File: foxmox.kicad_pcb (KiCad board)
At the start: 2 copper layers, 63.5 x 63.5 mm, 17 parts, among them P1 2.5mm plug, Q1 2N2222A, U1 PIC16F84, Y1 3.579MHz

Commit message: Slightly better PCB
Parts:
- D1: footprint Diode_SMD:D_MiniMELF -> Diode_THT:D_A-405_P10.16mm_Horizontal
- P1: footprint TerminalBlock:TerminalBlock_MaiXu_MX126-5.0-03P_1x03_P5.00mm -> TerminalBlock_CUI:TerminalBlock_CUI_TB007-508-03_1x03_P5.08mm_Horizontal
- R2: footprint Potentiometer_THT:Potentiometer_Piher_PT-15-H01_Horizontal -> Potentiometer_THT:Potentiometer_Bourns_3266W_Vertical
- moved C4 52.1 mm to (134.1, 67.5)
- moved S3 47.6 mm to (122.6, 68.4)
- moved Q1 37.1 mm to (143.0, 73.0)
- moved C3 31.4 mm to (149.5, 67.5)
- moved P1 28.9 mm to (120.0, 84.9), turned to -90 degrees
- moved D1 23.0 mm to (151.8, 92.5)
- moved R4 20.4 mm to (115.4, 101.5)
- moved R2 18.7 mm to (158.8, 67.5), turned to 90 degrees
- moved Y1 18.3 mm to (159.1, 99.5)
- moved R3 12.8 mm to (149.9, 85.5)
- moved R5 12.7 mm to (116.9, 78.0)
- moved U1 12.3 mm to (136.2, 79.8)
- moved C1 12.0 mm to (150.0, 97.4)
- moved S1 11.7 mm to (125.0, 110.0)
- moved C2 9.17 mm to (150.0, 101.5)
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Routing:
- net Net-(D1-K): track 0.00 -> 64.8 mm, vias 0 -> 1
- net Net-(Q1-PadC): track 0.00 -> 52.3 mm
- net Net-(C4-Pad2): track 0.00 -> 47.3 mm
- net Net-(U1-OSC1/CLKIN): track 0.00 -> 31.2 mm
- net Net-(C4-Pad1): track 0.00 -> 30.0 mm
- net Net-(Q1-PadB): track 0.00 -> 30.0 mm
- net Net-(S3-C): track 0.00 -> 26.5 mm
- net Net-(U1-OSC2/CLKOUT): track 0.00 -> 25.0 mm
- net Net-(U1-INT/RB0): track 0.00 -> 24.6 mm
- net Net-(U1-RB7): track 0.00 -> 23.9 mm
- net Net-(U1-RB2): track 0.00 -> 22.0 mm
- net Net-(U1-RB5): track 0.00 -> 21.4 mm
- net Net-(U1-RB6): track 0.00 -> 21.3 mm
- net Net-(U1-RB1): track 0.00 -> 21.3 mm
- net Net-(U1-RA3): track 0.00 -> 21.1 mm
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- added copper zone on B.Cu, net GNDREF
- added copper zone on F.Cu, net GNDREF
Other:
- board size 63.5 x 63.5 mm -> 60 x 60 mm

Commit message: Add datasheets and libraries for chosen components
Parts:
- added H1: MountingHole, MountingHole:MountingHole_2.5mm, F.Cu at (113.0, 63.0)
- added H2: MountingHole, MountingHole:MountingHole_2.5mm, F.Cu at (167.0, 63.0)
- added H3: MountingHole, MountingHole:MountingHole_2.5mm, F.Cu at (113.0, 117.0)
- added H4: MountingHole, MountingHole:MountingHole_2.5mm, F.Cu at (167.0, 117.0)
- S1, S2: footprint Button_Switch_SMD:Nidec_Copal_SH-7040B -> RDS5_16S_1065_D_67:SW_RDS5-16S-1065-D-67
- S3: footprint Button_Switch_THT:SW_E-Switch_EG1271_SPDT -> Button_Switch_THT:SW_CK_JS202011CQN_DPDT_Straight
- Y1: footprint Crystal:Crystal_HC52-6mm_Vertical -> Crystal:Crystal_HC49-4H_Vertical
- moved S2 4.78 mm to (151.0, 107.5)
- moved S1 4.36 mm to (121.5, 107.5)
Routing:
- net Net-(U1-OSC1/CLKIN): track 31.2 -> 32.3 mm

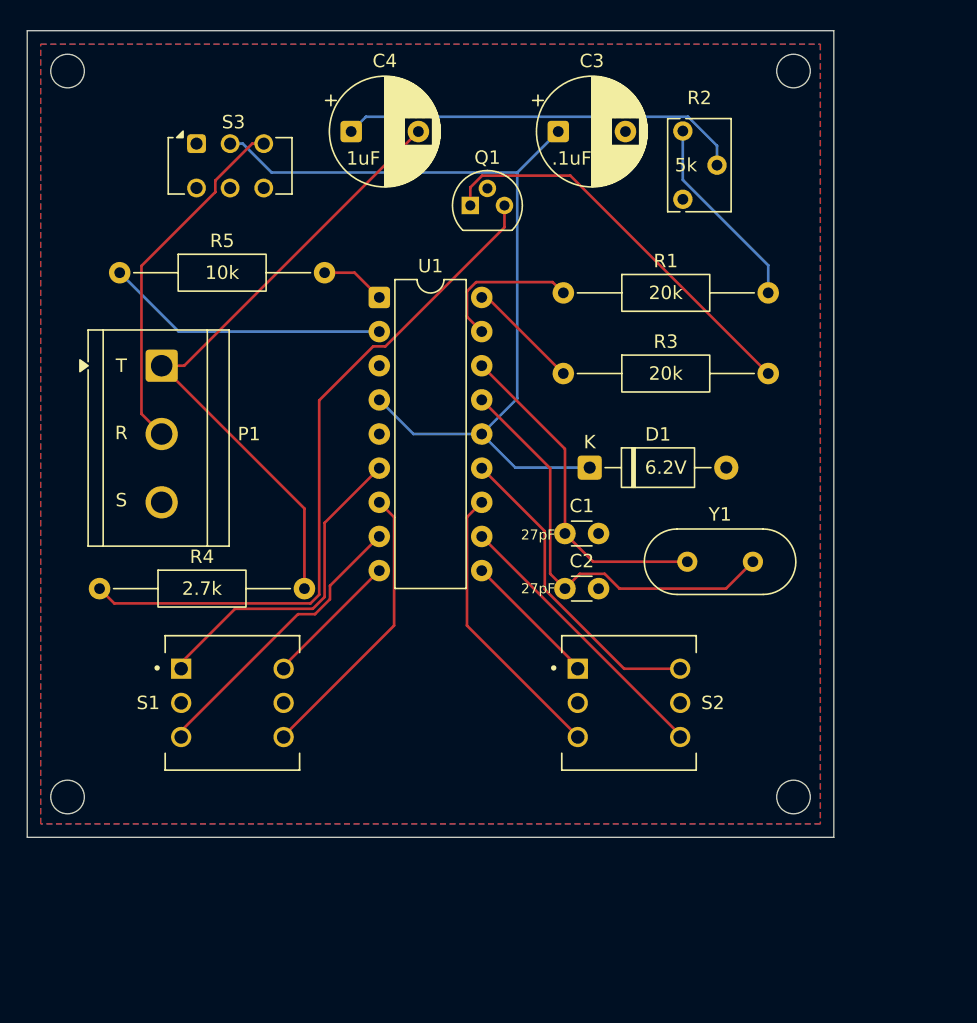
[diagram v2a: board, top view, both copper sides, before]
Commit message: Smaller PCB
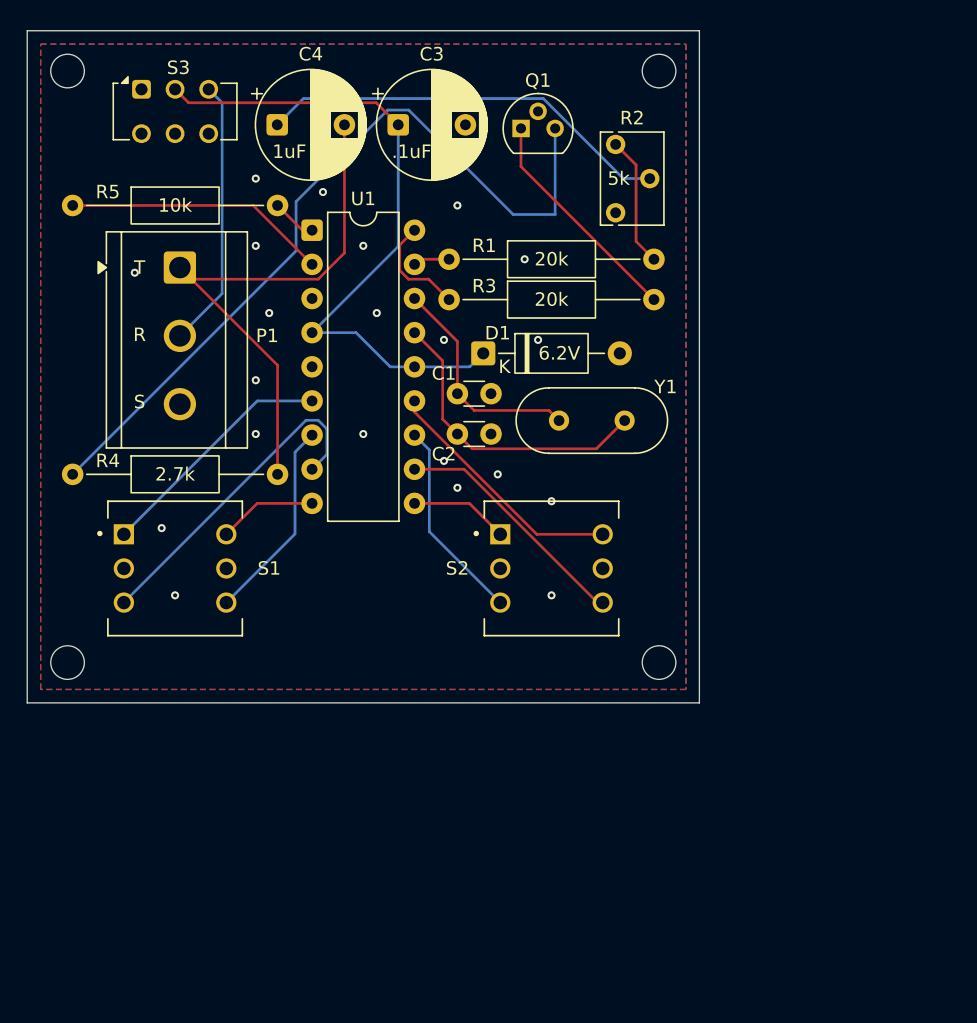
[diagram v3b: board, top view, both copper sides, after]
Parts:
- moved Y1 14.2 mm to (149.6, 89.0)
- moved H4 14.1 mm to (157.0, 107.0)
- moved C2 14.0 mm to (142.0, 90.0)
- moved C1 13.1 mm to (142.0, 87.0)
- moved C3 11.9 mm to (137.6, 67.0)
- moved D1 11.6 mm to (143.9, 84.0)
- moved R3 10.1 mm to (141.4, 80.0)
- moved H2 10.0 mm to (157.0, 63.0)
- moved H3 10.0 mm to (113.0, 107.0)
- moved R1 8.86 mm to (141.4, 77.0)
- moved R4 8.73 mm to (113.4, 93.0)
- moved S2 7.71 mm to (149.0, 100.0)
- moved S1 7.47 mm to (121.0, 100.0)
- moved P1 7.43 mm to (121.4, 77.6)
- moved U1 7.07 mm to (131.2, 74.8)
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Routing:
- net Net-(D1-K): track 64.8 -> 50.0 mm
- net Net-(Q1-PadB): track 30.0 -> 16.8 mm
- net Net-(U1-OSC1/CLKIN): track 32.3 -> 22.6 mm
- net Net-(U1-RA0): track 11.2 -> 2.73 mm
- net Net-(U1-OSC2/CLKOUT): track 25.0 -> 16.8 mm
- net Net-(Q1-PadC): track 52.3 -> 58.9 mm
- net Net-(U1-INT/RB0): track 24.6 -> 18.1 mm
- net Net-(S3-C): track 26.5 -> 20.1 mm
- net Net-(U1-RB6): track 21.3 -> 15.1 mm, vias 0 -> 1
- net Net-(U1-RB1): track 21.3 -> 15.1 mm
- net Net-(C4-Pad2): track 47.3 -> 41.3 mm
- net Net-(U1-RB7): track 23.9 -> 18.6 mm
- net Net-(R1-Pad2): track 14.7 -> 9.72 mm
- net Net-(U1-RB5): track 21.4 -> 18.1 mm
- net Net-(U1-RB4): track 10.3 -> 7.33 mm
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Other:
- board size 60 x 60 mm -> 50 x 50 mm
- board text added: "${TITLE} ${REVISION} ${ISSUE_DATE} ${COMPANY} ${COMMENT1}"

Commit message: Slightly thicker power traces
And possibly fix transistor pins
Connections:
- net Net-(D1-K) renamed /VDD
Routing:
- net Net-(Q1-PadC): track 58.9 -> 46.5 mm
- net Net-(Q1-PadB): track 16.8 -> 17.6 mm
- net /VDD: track 50.0 -> 50.6 mm, vias 1 -> 0
- net Net-(U1-RB6): vias 1 -> 0
- net Net-(U1-RB3): vias 1 -> 0
- net GNDREF: vias 21 -> 24
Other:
- board text added: "${ISSUE_DATE} ${COMPANY} ${COMMENT1}"
- board text added: "${TITLE} ${REVISION}"
- board text removed: "${TITLE} ${REVISION} ${ISSUE_DATE} ${COMPANY} ${COMMENT1}"

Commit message: Adjust some parts, footprints, etc
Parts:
- added TP1: VDD, TestPoint:TestPoint_Pad_D2.0mm, F.Cu at (128.5, 66.5)
- C1, C2: footprint Capacitor_THT:C_Disc_D3.0mm_W1.6mm_P2.50mm -> Capacitor_THT:C_Disc_D4.3mm_W1.9mm_P5.00mm
- C3, C4: footprint Capacitor_THT:CP_Radial_D8.0mm_P5.00mm -> Capacitor_THT:C_Disc_D4.3mm_W1.9mm_P5.00mm
- D1: footprint Diode_THT:D_A-405_P10.16mm_Horizontal -> Diode_THT:D_DO-35_SOD27_P7.62mm_Horizontal
- H1, H2, H3, H4: footprint MountingHole:MountingHole_2.5mm -> MountingHole:MountingHole_2.5mm_Pad
- Q1: footprint Package_TO_SOT_THT:TO-92 -> Package_TO_SOT_THT:TO-92_Inline_Wide
- S3: footprint Button_Switch_THT:SW_CK_JS202011CQN_DPDT_Straight -> EG1218:SW_1218_EWI
- moved R2 11.2 mm to (143.0, 65.5)
- moved Y1 6.47 mm to (155.0, 85.5), turned to -90 degrees
- moved C3 5.48 mm to (132.5, 69.0)
- moved C4 4.63 mm to (132.5, 64.5)
- moved Q1 4.59 mm to (150.4, 70.0)
- moved S3 3.78 mm to (117.5, 68.0), turned to 90 degrees
- moved D1 1.23 mm to (142.7, 84.0)
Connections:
- R3 pad 2: Net-(Q1-PadB) -> Net-(Q1-B)
- R4 pad 1: Net-(Q1-PadC) -> Net-(Q1-C)
- U1 pad 15: Net-(U1-OSC1/CLKIN) -> Net-(U1-OSC2/CLKOUT)
- U1 pad 16: Net-(U1-OSC2/CLKOUT) -> Net-(U1-OSC1/CLKIN)
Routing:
- net Net-(Q1-C): track 0.00 -> 51.6 mm
- net Net-(Q1-PadC): track 46.5 -> 0.00 mm
- net Net-(Q1-PadB): track 17.6 -> 0.00 mm
- net Net-(C4-Pad1): track 31.1 -> 14.4 mm
- net Net-(Q1-B): track 0.00 -> 12.4 mm
- net /VDD: track 50.6 -> 40.8 mm
- net Net-(R1-Pad2): track 9.72 -> 18.9 mm
- net Net-(U1-RB2): track 24.4 -> 18.7 mm
- net Net-(S3-C): track 20.1 -> 16.4 mm
- net Net-(U1-OSC1/CLKIN): track 22.7 -> 26.1 mm
- net Net-(U1-OSC2/CLKOUT): track 16.9 -> 19.5 mm, vias 0 -> 1
- net Net-(U1-RA1): track 8.02 -> 6.22 mm, vias 0 -> 1
- net Net-(U1-RB6): track 15.1 -> 16.6 mm
- net Net-(U1-RB1): track 15.1 -> 16.6 mm
- net Net-(U1-RA3): track 19.6 -> 21.1 mm
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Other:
- board text added: "OFF ON"

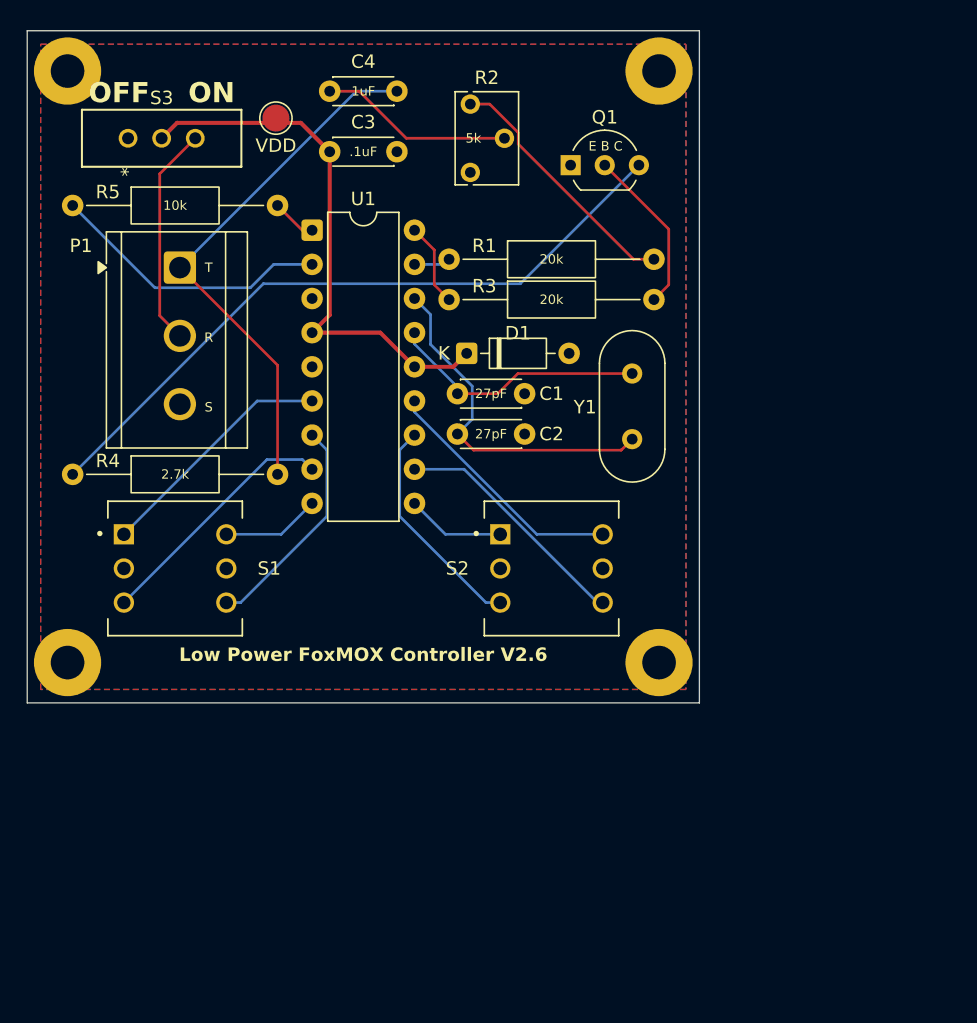
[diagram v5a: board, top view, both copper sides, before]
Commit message: Change 2.5mm terminal block and add strain relief
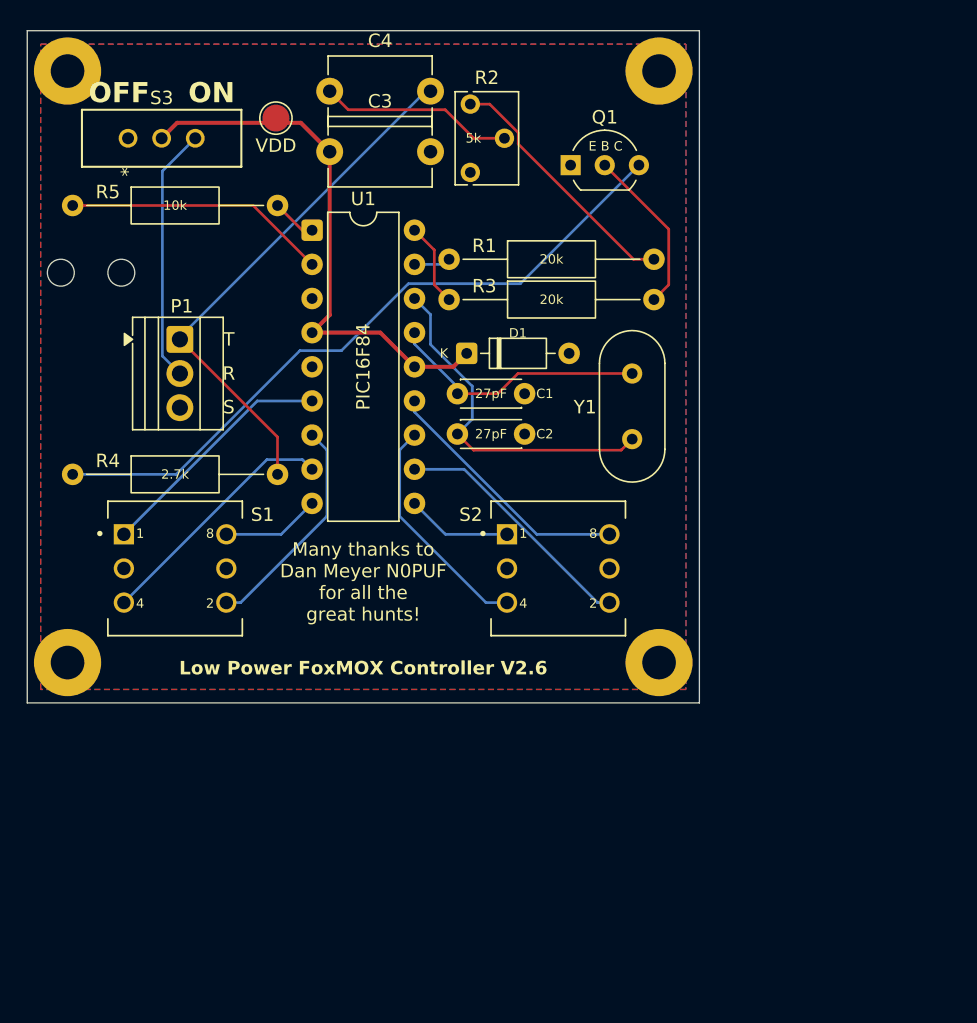
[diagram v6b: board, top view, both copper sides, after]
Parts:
- added H5: MountingHole, MountingHole:MountingHole_2mm, F.Cu at (112.5, 78.0)
- added H6: MountingHole, MountingHole:MountingHole_2mm, F.Cu at (117.0, 78.0)
- C3, C4: footprint Capacitor_THT:C_Disc_D4.3mm_W1.9mm_P5.00mm -> Capacitor_THT:C_Disc_D7.5mm_W5.0mm_P7.50mm
- P1: footprint TerminalBlock_CUI:TerminalBlock_CUI_TB007-508-03_1x03_P5.08mm_Horizontal -> TerminalBlock:TerminalBlock_Xinya_XY308-2.54-3P_1x03_P2.54mm_Horizontal
- moved P1 5.34 mm to (121.4, 83.0)
- moved S2 0.50 mm to (149.5, 100.0)
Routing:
- net Net-(S3-C): track 16.4 -> 19.1 mm
- net Net-(U1-RA3): track 21.1 -> 19.6 mm, vias 0 -> 1
- net Net-(C4-Pad2): track 40.0 -> 39.4 mm, vias 1 -> 0
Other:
- board text added: "Many thanks to Dan Meyer N0PUF for all the great hunts!"
